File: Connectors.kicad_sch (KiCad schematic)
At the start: 9 parts, among them J1 Screw_Terminal_01x02, J2 Screw_Terminal_01x02, J3 Screw_Terminal_01x02, J4 Screw_Terminal_01x02, J5 Screw_Terminal_01x02

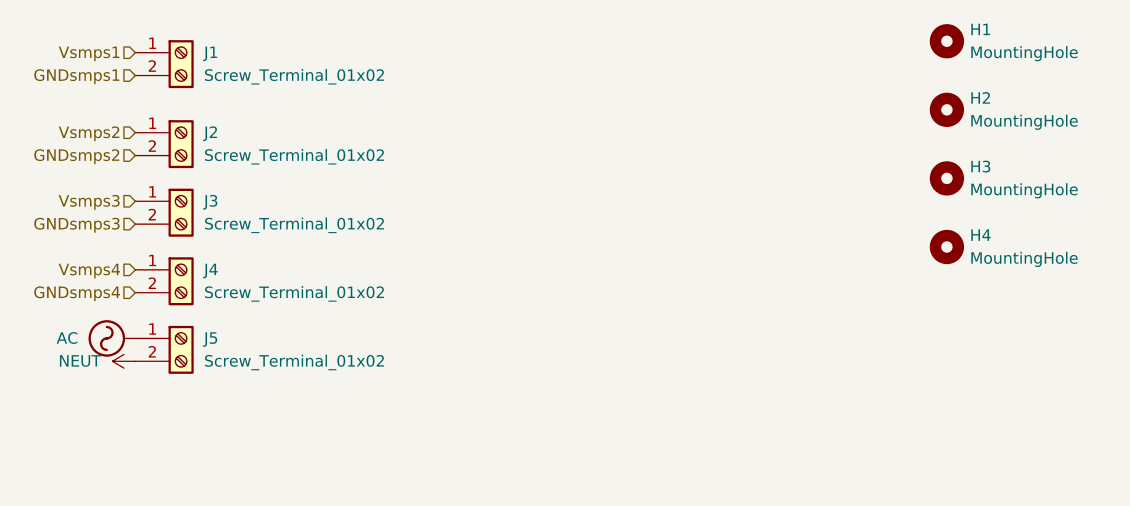
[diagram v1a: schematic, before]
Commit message: dev: added NC flags and fixed ERC warnings. Added custom design rules for PCB Design.
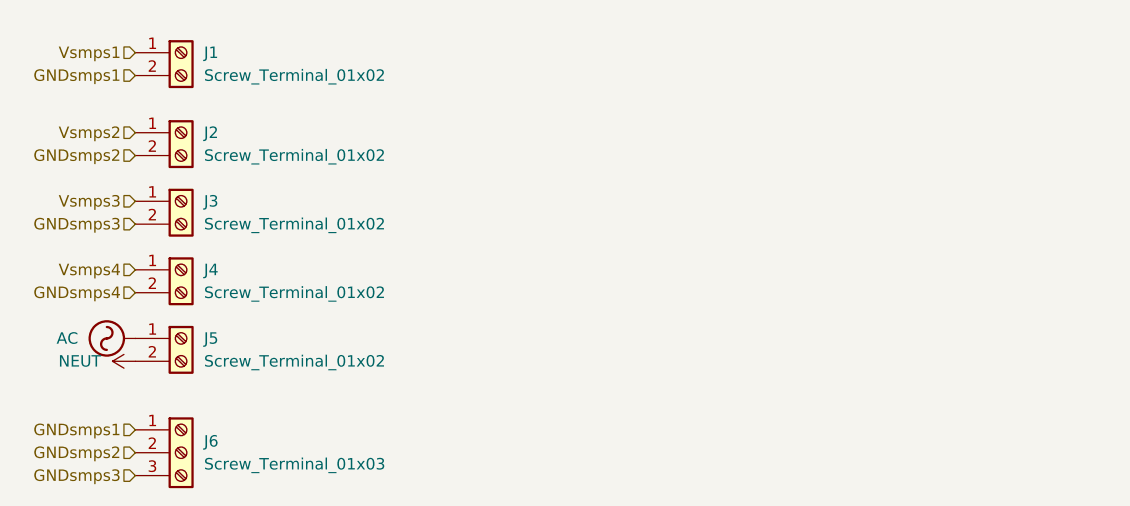
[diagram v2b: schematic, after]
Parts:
- removed H1, H2, H3, H4: MountingHole, symbol Mechanical:MountingHole
- added J6: Screw_Terminal_01x03, Connector_Phoenix_GMSTB:PhoenixContact_GMSTBVA_2,5_3-G-7,62_1x03_P7.62mm_Vertical, symbol Connector:Screw_Terminal_01x03
- J1, J2, J3, J4, J5: footprint (none) -> Connector_Phoenix_GMSTB:PhoenixContact_GMSTBVA_2,5_2-G-7,62_1x02_P7.62mm_Vertical
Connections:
- net GNDsmps1: now also J6.1 (Pin_1)
- net GNDsmps2: now also J6.2 (Pin_2)
- net GNDsmps3: now also J6.3 (Pin_3)
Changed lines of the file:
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@@
 		(rev "2")
 	)
+	(hierarchical_label "GNDsmps2"
+		(shape input)
+		(at 96.52 109.22 180)
+		(effects
+			(font
+				(size 1.27 1.27)
+			)
+			(justify right)
+		)
+	)
 	(hierarchical_label "Vsmps1"
 		(shape input)
@@
 		)
 	)
+	(hierarchical_label "GNDsmps3"
+		(shape input)
+		(at 96.52 111.76 180)
+		(effects
+			(font
+				(size 1.27 1.27)
+			)
+			(justify right)
+		)
+	)
 	(hierarchical_label "Vsmps2"
 		(shape input)
@@
 	(hierarchical_label "GNDsmps1"
 		(shape input)
+		(at 96.52 106.68 180)
+		(effects
+			(font
+				(size 1.27 1.27)
+			)
+			(justify right)
+		)
+	)
+	(hierarchical_label "GNDsmps1"
+		(shape input)
 		(at 96.52 67.31 180)
 		(effects
@@
 			)
 			(justify right)
-		)
-	)
-	(symbol
-		(lib_id "Mechanical:MountingHole")
-		(at 186.69 63.5 0)
-		(unit 1)
-		(exclude_from_sim no)
-		(in_bom no)
-		(on_board yes)
-		(dnp no)
-		(fields_autoplaced yes)
-		(property "Reference" "H1"
-			(at 189.23 62.2299 0)
-			(effects
-				(font
-					(size 1.27 1.27)
-				)
-				(justify left)
-			)
-		)
-		(property "Value" "MountingHole"
-			(at 189.23 64.7699 0)
-			(effects
-				(font
-					(size 1.27 1.27)
-				)
-				(justify left)
-			)
-		)
-		(property "Footprint" ""
-			(at 186.69 63.5 0)
-			(effects
-				(font
-					(size 1.27 1.27)
-				)
-				(hide yes)
-			)
-		)
-		(property "Datasheet" "~"
-			(at 186.69 63.5 0)
-			(effects
-				(font
-					(size 1.27 1.27)
-				)
-				(hide yes)
-			)
-		)
-		(property "Description" "Mounting Hole without connection"
-			(at 186.69 63.5 0)
-			(effects
-				(font
-					(size 1.27 1.27)
-				)
-				(hide yes)
-			)
-		)
-		(instances
-			(project ""
-				(path "/6a7e1a19-486b-4340-90f8-1e7274261ff8/8a931727-0f0a-4405-8b09-956dec8ed6bf"
-					(reference "H1")
-					(unit 1)
-				)
-			)
-		)
-	)
-	(symbol
-		(lib_id "Mechanical:MountingHole")
-		(at 186.69 71.12 0)
-		(unit 1)
-		(exclude_from_sim no)
-		(in_bom no)
-		(on_board yes)
-		(dnp no)
-		(fields_autoplaced yes)
-		(property "Reference" "H2"
-			(at 189.23 69.8499 0)
-			(effects
-				(font
-					(size 1.27 1.27)
-				)
-				(justify left)
-			)
-		)
-		(property "Value" "MountingHole"
-			(at 189.23 72.3899 0)
-			(effects
-				(font
-					(size 1.27 1.27)
-				)
-				(justify left)
-			)
-		)
-		(property "Footprint" ""
-			(at 186.69 71.12 0)
-			(effects
-				(font
-					(size 1.27 1.27)
-				)
-				(hide yes)
-			)
-		)
-		(property "Datasheet" "~"
-			(at 186.69 71.12 0)
-			(effects
-				(font
-					(size 1.27 1.27)
-				)
-				(hide yes)
-			)
-		)
-		(property "Description" "Mounting Hole without connection"
-			(at 186.69 71.12 0)
-			(effects
-				(font
-					(size 1.27 1.27)
-				)
-				(hide yes)
-			)
-		)
-		(instances
-			(project "inverter"
-				(path "/6a7e1a19-486b-4340-90f8-1e7274261ff8/8a931727-0f0a-4405-8b09-956dec8ed6bf"
-					(reference "H2")
-					(unit 1)
-				)
-			)
 		)
 	)
@@
 			)
 		)
-		(property "Footprint" ""
+		(property "Footprint" "Connector_Phoenix_GMSTB:PhoenixContact_GMSTBVA_2,5_2-G-7,62_1x02_P7.62mm_Vertical"
 			(at 101.6 81.28 0)
 			(effects
@@
 			)
 		)
-		(property "Footprint" ""
+		(property "Footprint" "Connector_Phoenix_GMSTB:PhoenixContact_GMSTBVA_2,5_2-G-7,62_1x02_P7.62mm_Vertical"
 			(at 101.6 88.9 0)
 			(effects
@@
 	)
 	(symbol
+		(lib_id "Connector:Screw_Terminal_01x03")
+		(at 101.6 109.22 0)
+		(unit 1)
+		(exclude_from_sim no)
+		(in_bom yes)
+		(on_board yes)
+		(dnp no)
+		(fields_autoplaced yes)
+		(property "Reference" "J6"
+			(at 104.14 107.9499 0)
+			(effects
+				(font
+					(size 1.27 1.27)
+				)
+				(justify left)
+			)
+		)
+		(property "Value" "Screw_Terminal_01x03"
+			(at 104.14 110.4899 0)
+			(effects
+				(font
+					(size 1.27 1.27)
+				)
+				(justify left)
+			)
+		)
+		(property "Footprint" "Connector_Phoenix_GMSTB:PhoenixContact_GMSTBVA_2,5_3-G-7,62_1x03_P7.62mm_Vertical"
+			(at 101.6 109.22 0)
+			(effects
+				(font
+					(size 1.27 1.27)
+				)
+				(hide yes)
+			)
+		)
+		(property "Datasheet" "~"
+			(at 101.6 109.22 0)
+			(effects
+				(font
+					(size 1.27 1.27)
+				)
+				(hide yes)
+			)
+		)
+		(property "Description" "Generic screw terminal, single row, 01x03, script generated (kicad-library-utils/schlib/autogen/connector/)"
+			(at 101.6 109.22 0)
+			(effects
+				(font
+					(size 1.27 1.27)
+				)
+				(hide yes)
+			)
+		)
+		(pin "1"
+		)
+		(pin "3"
+		)
+		(pin "2"
+		)
+		(instances
+			(project ""
+				(path "/6a7e1a19-486b-4340-90f8-1e7274261ff8/8a931727-0f0a-4405-8b09-956dec8ed6bf"
+					(reference "J6")
+					(unit 1)
+				)
+			)
+		)
+	)
+	(symbol
 		(lib_id "Connector:Screw_Terminal_01x02")
 		(at 101.6 73.66 0)
@@
 			)
 		)
-		(property "Footprint" ""
+		(property "Footprint" "Connector_Phoenix_GMSTB:PhoenixContact_GMSTBVA_2,5_2-G-7,62_1x02_P7.62mm_Vertical"
 			(at 101.6 73.66 0)
 			(effects
@@
 	)
 	(symbol
-		(lib_id "Mechanical:MountingHole")
-		(at 186.69 86.36 0)
-		(unit 1)
-		(exclude_from_sim no)
-		(in_bom no)
-		(on_board yes)
-		(dnp no)
-		(fields_autoplaced yes)
-		(property "Reference" "H4"
-			(at 189.23 85.0899 0)
-			(effects
-				(font
-					(size 1.27 1.27)
-				)
-				(justify left)
-			)
-		)
-		(property "Value" "MountingHole"
-			(at 189.23 87.6299 0)
-			(effects
-				(font
-					(size 1.27 1.27)
-				)
-				(justify left)
-			)
-		)
-		(property "Footprint" ""
-			(at 186.69 86.36 0)
-			(effects
-				(font
-					(size 1.27 1.27)
-				)
-				(hide yes)
-			)
-		)
-		(property "Datasheet" "~"
-			(at 186.69 86.36 0)
-			(effects
-				(font
-					(size 1.27 1.27)
-				)
-				(hide yes)
-			)
-		)
-		(property "Description" "Mounting Hole without connection"
-			(at 186.69 86.36 0)
-			(effects
-				(font
-					(size 1.27 1.27)
-				)
-				(hide yes)
-			)
-		)
-		(instances
-			(project "inverter"
-				(path "/6a7e1a19-486b-4340-90f8-1e7274261ff8/8a931727-0f0a-4405-8b09-956dec8ed6bf"
-					(reference "H4")
-					(unit 1)
-				)
-			)
-		)
-	)
-	(symbol
 		(lib_id "power:NEUT")
 		(at 96.52 99.06 90)
@@
 			)
 		)
-		(property "Footprint" ""
+		(property "Footprint" "Connector_Phoenix_GMSTB:PhoenixContact_GMSTBVA_2,5_2-G-7,62_1x02_P7.62mm_Vertical"
 			(at 101.6 96.52 0)
 			(effects
@@
 			)
 		)
-		(property "Footprint" ""
+		(property "Footprint" "Connector_Phoenix_GMSTB:PhoenixContact_GMSTBVA_2,5_2-G-7,62_1x02_P7.62mm_Vertical"
 			(at 101.6 64.77 0)
 			(effects
@@
 					(unit 1)
 				)
-			)
-		)
-	)
-	(symbol
-		(lib_id "Mechanical:MountingHole")
-		(at 186.69 78.74 0)
-		(unit 1)
-		(exclude_from_sim no)
-		(in_bom no)
-		(on_board yes)
-		(dnp no)
-		(fields_autoplaced yes)
-		(property "Reference" "H3"
-			(at 189.23 77.4699 0)
-			(effects
-				(font
-					(size 1.27 1.27)
-				)
-				(justify left)
-			)
-		)
-		(property "Value" "MountingHole"
-			(at 189.23 80.0099 0)
-			(effects
-				(font
-					(size 1.27 1.27)
-				)
-				(justify left)
-			)
-		)
-		(property "Footprint" ""
-			(at 186.69 78.74 0)
-			(effects
-				(font
-					(size 1.27 1.27)
-				)
-				(hide yes)
-			)
-		)
-		(property "Datasheet" "~"
-			(at 186.69 78.74 0)
-			(effects
-				(font
-					(size 1.27 1.27)
-				)
-				(hide yes)
-			)
-		)
-		(property "Description" "Mounting Hole without connection"
-			(at 186.69 78.74 0)
-			(effects
-				(font
-					(size 1.27 1.27)
-				)
-				(hide yes)
-			)
-		)
-		(instances
-			(project "inverter"
-				(path "/6a7e1a19-486b-4340-90f8-1e7274261ff8/8a931727-0f0a-4405-8b09-956dec8ed6bf"
-					(reference "H3")
-					(unit 1)
-				)
